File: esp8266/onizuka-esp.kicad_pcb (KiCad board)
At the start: 2 copper layers, 50 x 50 mm, 14 parts, among them P1 FTDI_CONN, U1 ESP-01, U2 ESP-12E, U3 ESP-02

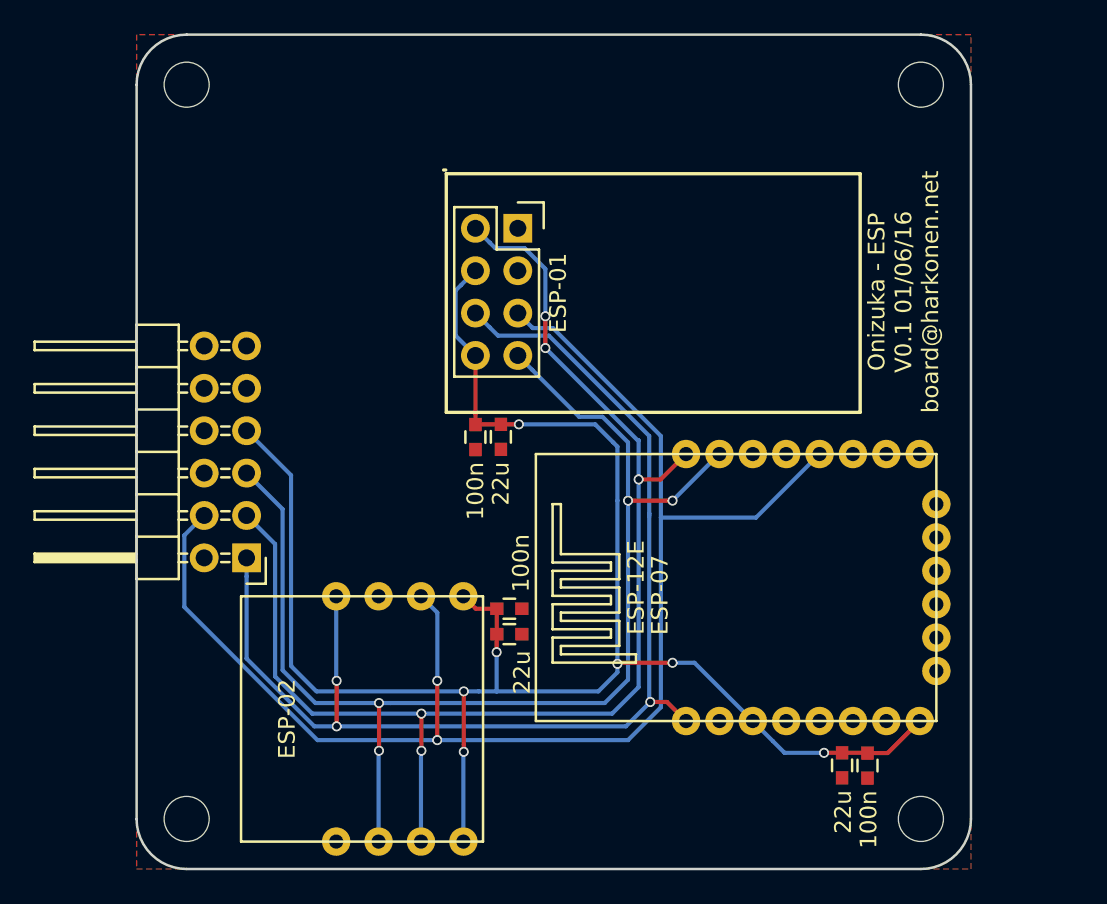
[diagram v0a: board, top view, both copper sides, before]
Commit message: ESP board rearrainge, also logo.
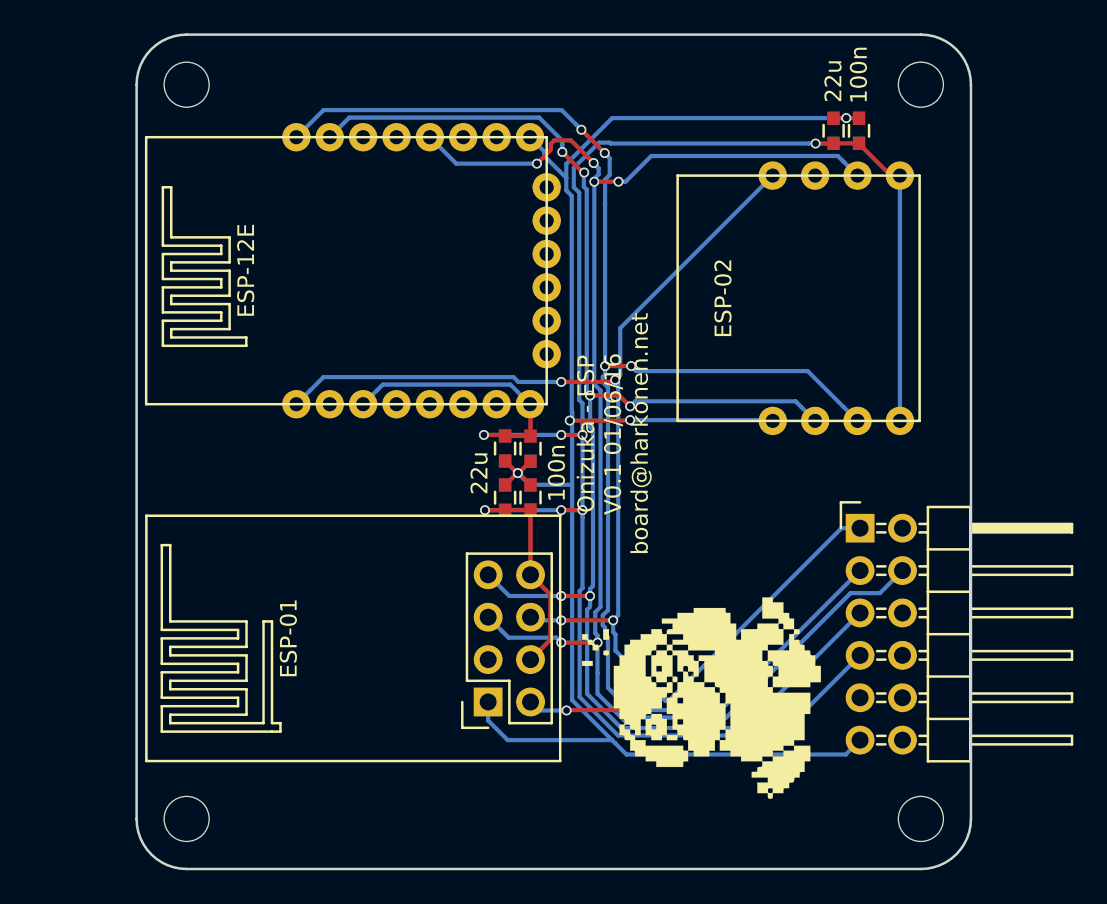
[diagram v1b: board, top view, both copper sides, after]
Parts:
- added G***: LOGO, LOGO, F.Cu at (49.0, 53.5)
- U1: footprint Socket_Strips:Socket_Strip_Straight_2x04 -> ESP:ESP-01
- moved P1 36.8 mm to (58.4, 44.6), turned to 0 degrees
- moved U3 36.3 mm to (54.7, 30.8)
- moved C7 35.9 mm to (56.8, 20.8), turned to 90 degrees
- moved C6 35.5 mm to (58.3, 20.8), turned to 90 degrees
- moved U2 30.1 mm to (27.6, 29.1)
- moved C4 27.7 mm to (38.6, 39.8)
- moved C3 27.7 mm to (37.1, 39.8)
- moved U1 24.6 mm to (37.3, 51.2), turned to 90 degrees
- moved C1 4.90 mm to (38.6, 42.7), turned to 90 degrees
- moved C2 3.65 mm to (37.1, 42.7), turned to 90 degrees
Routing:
- net GND: track 0.00 -> 103.5 mm, vias 0 -> 4
- net VCC: track 106.1 -> 127.6 mm
- net /TXD: track 72.7 -> 90.2 mm, vias 4 -> 6
- net /RXD: track 77.5 -> 94.8 mm, vias 5 -> 6
- net /RTS: track 72.5 -> 77.8 mm, vias 3 -> 4
- net /DTR: track 86.6 -> 90.9 mm, vias 2 -> 6
- removed copper zone on F.Cu, net GND
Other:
- board text removed: "ESP-07"

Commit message: Final tweaks, more farnell part numbers, BOM, gerbers
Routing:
- net /RXD: track 94.8 -> 94.0 mm
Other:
- board text added: "Onizuka - ESP V1.0 04/06/16 board@harkonen.net"
- board text removed: "Onizuka - ESP V0.1 01/06/16 board@harkonen.net"
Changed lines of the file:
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@@
-(kicad_pcb (version 4) (host pcbnew 4.1.0-alpha+201605292346+6852~44~ubuntu16.04.1-product)
+(kicad_pcb (version 4) (host pcbnew "(2016-06-01 BZR 6870, Git 0ccd3bb)-product")
   (general
     (links 33)
-    (no_connects 1)
+    (no_connects 0)
     (area 14.924999 14.924999 65.075001 65.075001)
     (thickness 1.6)
     (drawings 9)
-    (tracks 252)
+    (tracks 253)
     (zones 0)
     (modules 15)
@@
     (visible_elements 7FFFFF7F)
     (pcbplotparams
-      (layerselection 0x00030_80000001)
-      (usegerberextensions false)
+      (layerselection 0x010fc_ffffffff)
+      (usegerberextensions true)
       (excludeedgelayer true)
-      (linewidth 0.100000)
+      (linewidth 0.150000)
       (plotframeref false)
       (viasonmask false)
@@
       (outputformat 1)
       (mirror false)
-      (drillshape 1)
+      (drillshape 0)
       (scaleselection 1)
-      (outputdirectory ""))
+      (outputdirectory gerbers/))
   )
   (net 0 "")
@@
   (gr_arc (start 62 18) (end 62 15) (angle 90) (layer Edge.Cuts) (width 0.15))
   (gr_arc (start 18 18) (end 15 18) (angle 90) (layer Edge.Cuts) (width 0.15))
-  (gr_text "Onizuka - ESP\nV0.1 01/06/16\nboard@harkonen.net" (at 43.561 38.9255 90) (layer F.SilkS)
+  (gr_text "Onizuka - ESP\nV1.0 04/06/16\nboard@harkonen.net" (at 43.561 38.9255 90) (layer F.SilkS)
     (effects (font (size 1 1) (thickness 0.15)))
   )
@@
   (segment (start 44.045293 56.551973) (end 42.000029 54.506709) (width 0.25) (layer B.Cu) (net 4))
   (segment (start 51.461527 56.551973) (end 44.045293 56.551973) (width 0.25) (layer B.Cu) (net 4))
+  (segment (start 43.250031 54.149991) (end 42.116009 54.149991) (width 0.25) (layer F.Cu) (net 5))
+  (segment (start 42.116009 54.149991) (end 40.767 55.499) (width 0.25) (layer F.Cu) (net 5))
+  (via (at 43.250031 54.149991) (size 0.6) (drill 0.4) (layers F.Cu B.Cu) (net 5))
   (segment (start 43.352999 22.397999) (end 43.053 22.098) (width 0.25) (layer B.Cu) (net 5))
   (segment (start 43.352999 23.412999) (end 43.352999 22.397999) (width 0.25) (layer B.Cu) (net 5))
@@
   (segment (start 40.767 55.499) (end 39.116 55.499) (width 0.25) (layer B.Cu) (net 5))
   (segment (start 39.116 55.499) (end 38.608 54.991) (width 0.25) (layer B.Cu) (net 5))
-  (segment (start 44.577 55.47696) (end 40.78904 55.47696) (width 0.25) (layer F.Cu) (net 5))
   (via (at 40.767 55.499) (size 0.6) (drill 0.4) (layers F.Cu B.Cu) (net 5))
   (segment (start 40.78904 55.47696) (end 40.767 55.499) (width 0.25) (layer F.Cu) (net 5))
-  (via (at 44.577 55.47696) (size 0.6) (drill 0.4) (layers F.Cu B.Cu) (net 5))
   (segment (start 58.3565 47.117) (end 49.99654 55.47696) (width 0.25) (layer B.Cu) (net 5))
   (segment (start 44.7675 55.47696) (end 44.577 55.47696) (width 0.25) (layer B.Cu) (net 5))
